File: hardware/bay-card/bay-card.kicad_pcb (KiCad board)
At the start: 4 copper layers, 40 x 37.6 mm, 39 parts, among them J1 bay card edge, J2 SATA 22-pin, Q1 AON7403, Q2 AON7403, Q3 2N7002, Q4 2N7002, U1 ASM1153E, Y1 30MHz CL=16pF

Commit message: hw(routing): close-gaps — grid A* router for the open connections the autorouter leaves; card down to 1 open (QFN pin 17 escape), DRC 0 errors
Co-Authored-By: Claude Sonnet 5 <noreply@anthropic.com>
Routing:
- net 5V_HDD: track 23.7 -> 49.3 mm, vias 14 -> 17
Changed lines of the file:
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@@
+	)
+	(segment
+		(start 32.47 53.08421)
+		(end 32.87 53.08421)
+		(width 0.3)
+		(layer "F.Cu")
+		(net 6)
 	)
 	(segment
@@
 	)
 	(segment
+		(start 24.17 48.88421)
+		(end 25.07 47.98421)
+		(width 0.3)
+		(layer "F.Cu")
+		(net 6)
+	)
+	(segment
+		(start 21.87 48.88421)
+		(end 24.17 48.88421)
+		(width 0.3)
+		(layer "F.Cu")
+		(net 6)
+	)
+	(segment
+		(start 32.47 52.98421)
+		(end 32.47 53.08421)
+		(width 0.3)
+		(layer "F.Cu")
+		(net 6)
+	)
+	(segment
 		(start 33.69 53.76)
 		(end 33.69 54.645)
@@
 	)
 	(segment
+		(start 31.17 51.68421)
+		(end 32.47 52.98421)
+		(width 0.3)
+		(layer "F.Cu")
+		(net 6)
+	)
+	(segment
 		(start 39 62.55)
 		(end 39 65.3)
@@
 	)
 	(segment
+		(start 21.87 53.08421)
+		(end 21.87 48.88421)
+		(width 0.3)
+		(layer "F.Cu")
+		(net 6)
+	)
+	(segment
 		(start 39.9 49.775)
 		(end 39.125 49.775)
@@
 	)
 	(segment
+		(start 25.97 47.98421)
+		(end 26.17 47.78421)
+		(width 0.3)
+		(layer "F.Cu")
+		(net 6)
+	)
+	(segment
 		(start 38 62.55)
 		(end 38 59.8)
@@
 	)
 	(segment
+		(start 25.07 47.98421)
+		(end 25.97 47.98421)
+		(width 0.3)
+		(layer "F.Cu")
+		(net 6)
+	)
+	(segment
 		(start 36.05 40.48)
 		(end 36.05 39.18)
@@
 	)
 	(segment
+		(start 32.87 53.08421)
+		(end 33.06421 53.13421)
+		(width 0.3)
+		(layer "F.Cu")
+		(net 6)
+	)
+	(segment
 		(start 22.42 53.77)
 		(end 21.525 53.77)
@@
 	)
 	(segment
+		(start 22.42 53.77)
+		(end 22.37 53.58421)
+		(width 0.3)
+		(layer "F.Cu")
+		(net 6)
+	)
+	(segment
 		(start 39.9 50.425)
 		(end 39.125 50.425)
@@
 	)
 	(segment
+		(start 22.37 53.58421)
+		(end 21.87 53.08421)
+		(width 0.3)
+		(layer "F.Cu")
+		(net 6)
+	)
+	(segment
 		(start 22.42 53.77)
 		(end 22.42 54.665)
@@
 	)
 	(via
+		(at 26.17 47.78421)
+		(size 0.6)
+		(drill 0.3)
+		(layers "F.Cu" "B.Cu")
+		(net 6)
+	)
+	(via
+		(at 31.17 51.68421)
+		(size 0.6)
+		(drill 0.3)
+		(layers "F.Cu" "B.Cu")
+		(net 6)
+	)
+	(via
 		(at 21.525 53.77)
 		(size 0.45)
@@
 	)
 	(via
+		(at 33.69 53.76)
+		(size 0.6)
+		(drill 0.3)
+		(layers "F.Cu" "B.Cu")
+		(net 6)
+	)
+	(via
 		(at 33.06421 53.13421)
 		(size 0.45)
@@
 		(drill 0.2)
 		(layers "F.Cu" "B.Cu")
+		(net 6)
+	)
+	(segment
+		(start 27.27 47.88421)
+		(end 30.47 51.08421)
+		(width 0.3)
+		(layer "B.Cu")
+		(net 6)
+	)
+	(segment
+		(start 34.74 52.525)
+		(end 35.94 51.325)
+		(width 0.3)
+		(layer "B.Cu")
+		(net 6)
+	)
+	(segment
+		(start 26.17 47.78421)
+		(end 26.27 47.88421)
+		(width 0.3)
+		(layer "B.Cu")
+		(net 6)
+	)
+	(segment
+		(start 38.84 51.325)
+		(end 38.94 51.225)
+		(width 0.3)
+		(layer "B.Cu")
+		(net 6)
+	)
+	(segment
+		(start 34.54 52.525)
+		(end 34.74 52.525)
+		(width 0.3)
+		(layer "B.Cu")
+		(net 6)
+	)
+	(segment
+		(start 30.57 51.08421)
+		(end 31.17 51.68421)
+		(width 0.3)
+		(layer "B.Cu")
+		(net 6)
+	)
+	(segment
+		(start 38.94 51.225)
+		(end 39.125 51.075)
+		(width 0.3)
+		(layer "B.Cu")
+		(net 6)
+	)
+	(segment
+		(start 26.27 47.88421)
+		(end 27.27 47.88421)
+		(width 0.3)
+		(layer "B.Cu")
 		(net 6)
 	)
@@
 	)
 	(segment
+		(start 34.24 53.225)
+		(end 34.24 52.825)
+		(width 0.3)
+		(layer "B.Cu")
+		(net 6)
+	)
+	(segment
+		(start 33.84 53.625)
+		(end 34.24 53.225)
+		(width 0.3)
+		(layer "B.Cu")
+		(net 6)
+	)
+	(segment
+		(start 34.24 52.825)
+		(end 34.54 52.525)
+		(width 0.3)
+		(layer "B.Cu")
+		(net 6)
+	)
+	(segment
+		(start 35.94 51.325)
+		(end 38.84 51.325)
+		(width 0.3)
+		(layer "B.Cu")
+		(net 6)
+	)
+	(segment
 		(start 38 62.55)
 		(end 38 59.8)
@@
 		(layer "B.Cu")
 		(net 6)
+	)
+	(segment
+		(start 30.47 51.08421)
+		(end 30.57 51.08421)
+		(width 0.3)
+		(layer "B.Cu")
+		(net 6)

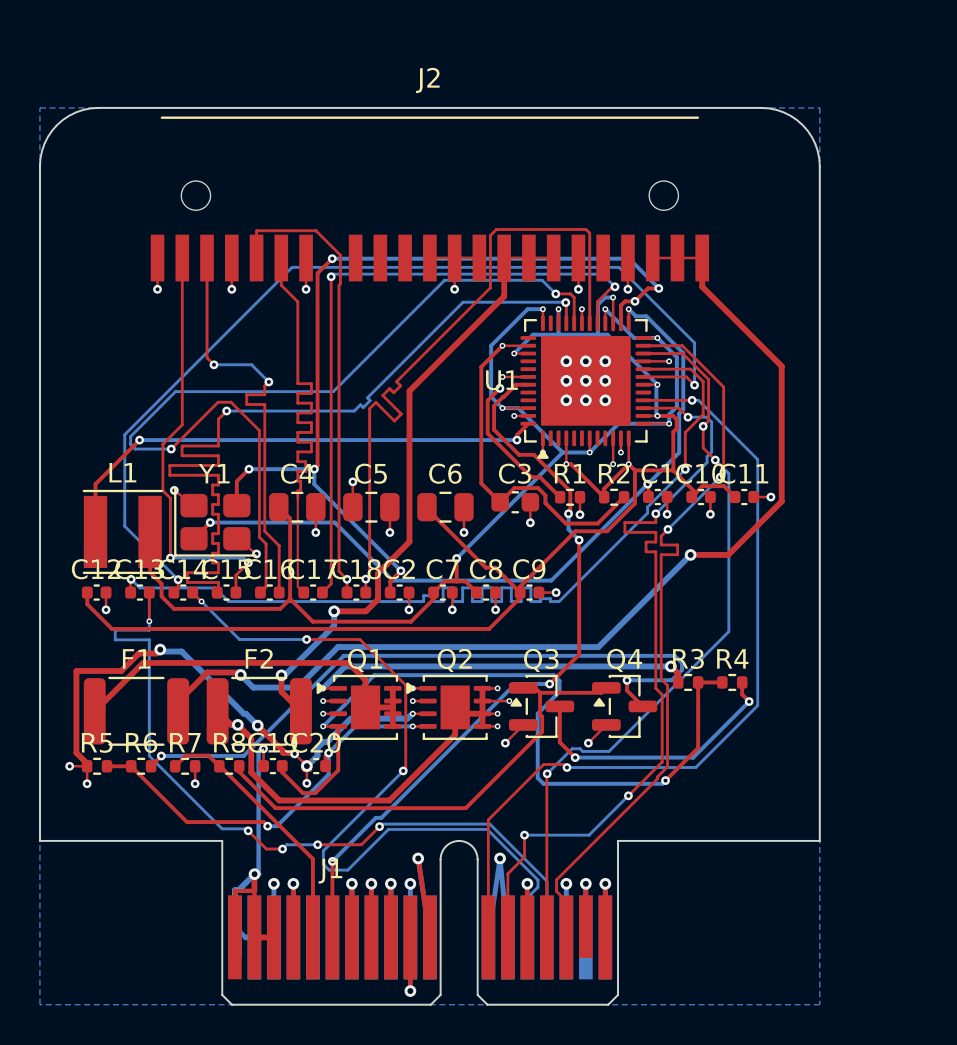
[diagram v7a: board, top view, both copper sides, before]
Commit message: hw: real Amphenol slot and Molex receptacle footprints, 45 mm bay card (C27, option A), enclosure rear extension and new lid windows; card 0 open, brain 5 open, DRC 0 errors
Co-Authored-By: Claude Sonnet 5 <noreply@anthropic.com>
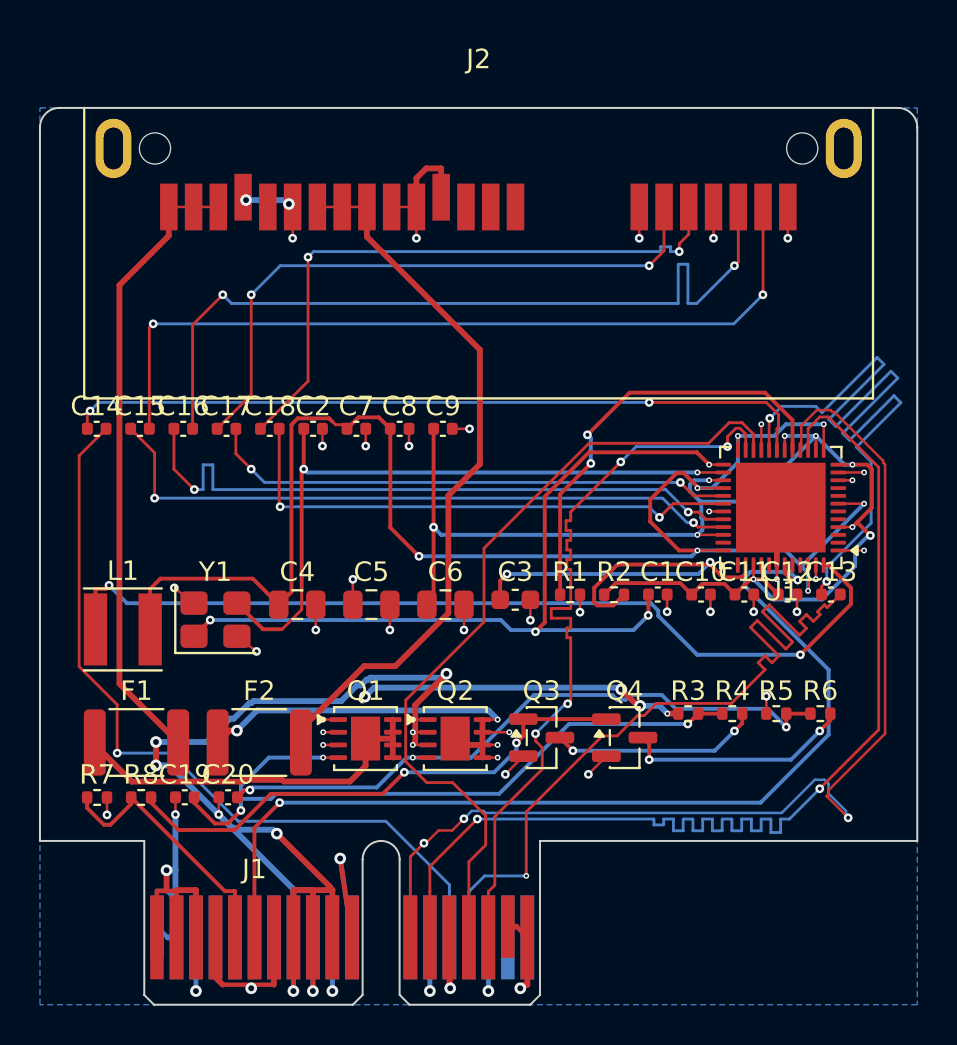
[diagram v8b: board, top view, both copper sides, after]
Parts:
- moved C12 35.4 mm to (58.4, 45.0)
- moved C13 35.4 mm to (60.6, 45.0)
- moved R5 34.9 mm to (57.8, 51.1)
- moved R6 34.9 mm to (60.0, 51.1)
- moved U1 11.9 mm to (58.0, 40.5), turned to 180 degrees
- moved C14 9.50 mm to (22.9, 36.5)
- moved C15 9.50 mm to (25.1, 36.5)
- moved C2 9.50 mm to (34.0, 36.5)
- moved C7 9.50 mm to (36.2, 36.5)
- moved C16 9.50 mm to (27.4, 36.5)
- moved C17 9.50 mm to (29.6, 36.5)
- moved C18 9.50 mm to (31.8, 36.5)
- moved C8 9.50 mm to (38.5, 36.5)
- moved C9 9.50 mm to (40.7, 36.5)
- moved J2 5.15 mm to (42.5, 20.0)
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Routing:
- net 5V_HDD: track 49.3 -> 76.4 mm, vias 17 -> 15
- net Q4_D: track 34.8 -> 11.7 mm
- net 12V_BAY: track 53.1 -> 32.3 mm, vias 2 -> 0
- net U1_LXI: track 26.1 -> 46.3 mm
- net SATA_A_P: track 21.9 -> 41.9 mm
- net SATA_A_N: track 21.9 -> 41.9 mm
- net USB2_DP: track 40.9 -> 57.0 mm, vias 4 -> 2
- net U1_VDD_CORE: track 66.6 -> 81.5 mm
- net U1_REXT: track 7.65 -> 22.5 mm, vias 1 -> 2
- net USB2_DM: track 42.1 -> 56.4 mm, vias 2 -> 3
- net LED_K: track 38.2 -> 51.1 mm, vias 4 -> 2
- net Q2_G: track 21.2 -> 33.9 mm
- net U1_STXN: track 45.0 -> 33.9 mm
- net U1_STXP: track 45.0 -> 33.9 mm
- net U1_XO: track 45.7 -> 35.2 mm, vias 6 -> 2
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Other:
- board size 40 x 37.6 mm -> 45 x 37.6 mm
- board text added: "brain-drain bay card v2 45x46"
- board text removed: "brain-drain bay card v1 40x46"
